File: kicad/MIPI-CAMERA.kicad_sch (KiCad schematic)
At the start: 12 parts, among them J4500 AXT530124

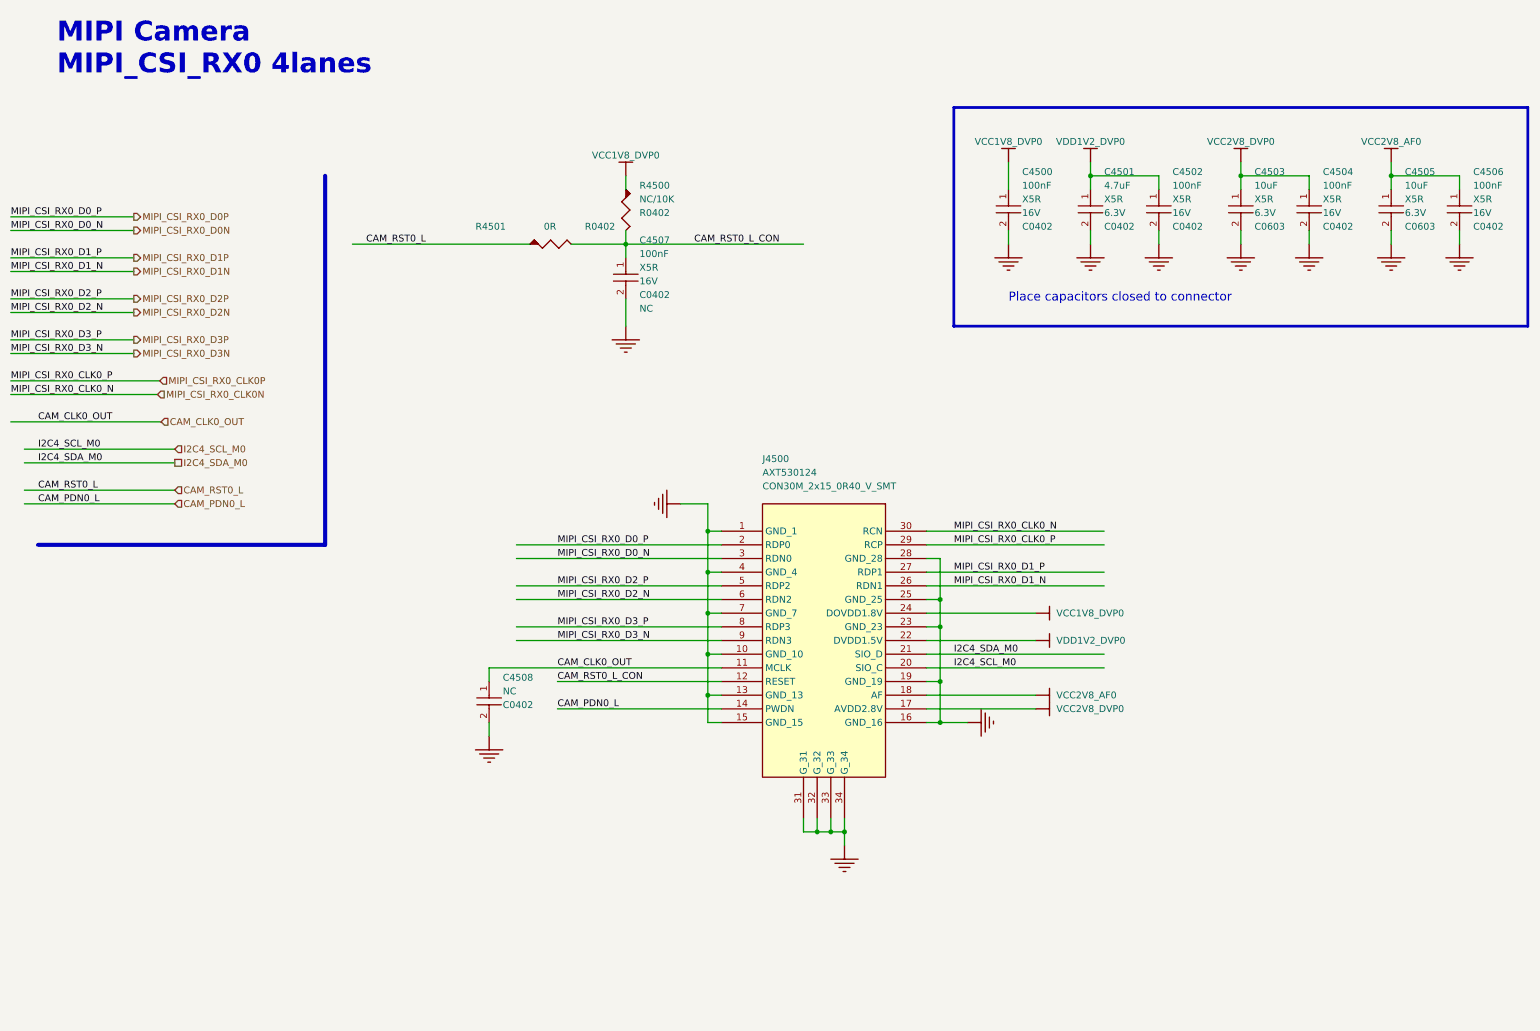
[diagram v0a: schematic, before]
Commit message: Added Pi CM4/CM5
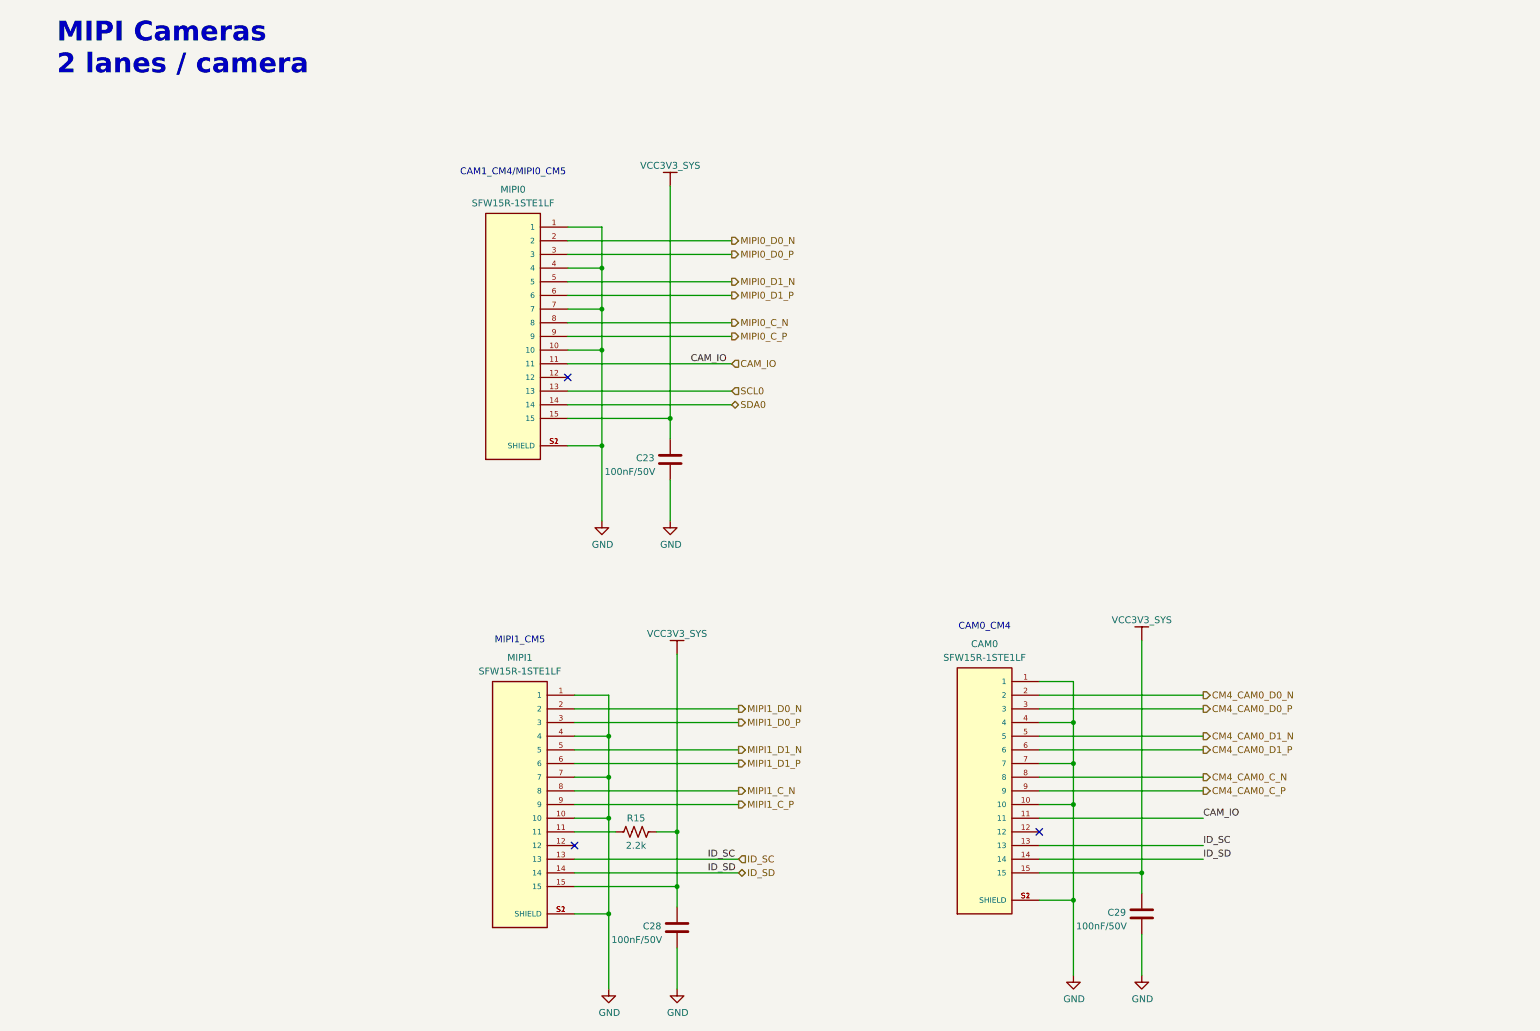
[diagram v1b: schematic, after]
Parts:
- removed C4500, C4502, C4504, C4506, C4507: 100nF, oomwoo_altium:C0402, symbol *:CAMERA_0_CAP NP_*
- removed C4501: 4.7uF, oomwoo_altium:C0402, symbol *:CAMERA_0_CAP NP_*
- removed C4503, C4505: 10uF, oomwoo_altium:C0603, symbol *:CAMERA_0_CAP NP_*
- removed C4508: NC, oomwoo_altium:C0402, symbol *:CAMERA_0_CAP NP_NC_*
- removed J4500: AXT530124, oomwoo_altium:CONN-SMD_30P-P0.40_AXT530124, symbol RK3562_REF:CAMERA_0_CMK-CB0077-FV1_2_RK3562_REF.SchLib
- removed R4500: NC/10K, Resistor_SMD:R_0402_1005Metric, symbol *:CAMERA_0_RESISTOR5_NC_*
- removed R4501: 0R, Resistor_SMD:R_0402_1005Metric, symbol *:CAMERA_1_RESISTOR5_*
- added C23, C28, C29: 100nF/50V, Capacitor_SMD:C_0603_1608Metric, symbol Device:C
- added CAM0, MIPI0, MIPI1: SFW15R-1STE1LF, SFW15R-1STE1LF:AMPHENOL_SFW15R-1STE1LF, symbol SFW15R-1STE1LF:SFW15R-1STE1LF
- added R15: 2.2k, symbol Device:R_US
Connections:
- net GND: now also C23.2, C28.2, C29.2, CAM0.1, CAM0.10, CAM0.4, CAM0.7, CAM0.S1 (SHIELD), CAM0.S2 (SHIELD), MIPI0.1, MIPI0.10, MIPI0.4, MIPI0.7, MIPI0.S1 (SHIELD), MIPI0.S2 (SHIELD), MIPI1.1, MIPI1.10, MIPI1.4, MIPI1.7, MIPI1.S1 (SHIELD), MIPI1.S2 (SHIELD)
- new net: MIPI1.11, R15.1
- new net CAM_IO: CAM0.11, MIPI0.11
- new net CM4_CAM0_C_N: CAM0.8
- new net CM4_CAM0_C_P: CAM0.9
- new net CM4_CAM0_D0_N: CAM0.2
- new net CM4_CAM0_D0_P: CAM0.3
- new net CM4_CAM0_D1_N: CAM0.5
- new net CM4_CAM0_D1_P: CAM0.6
- new net ID_SC: CAM0.13, MIPI1.13
- new net ID_SD: CAM0.14, MIPI1.14
- new net MIPI0_C_N: MIPI0.8
- new net MIPI0_C_P: MIPI0.9
- new net MIPI0_D0_N: MIPI0.2
- new net MIPI0_D0_P: MIPI0.3
- new net MIPI0_D1_N: MIPI0.5
- new net MIPI0_D1_P: MIPI0.6
- new net MIPI1_C_N: MIPI1.8
- new net MIPI1_C_P: MIPI1.9
- new net MIPI1_D0_N: MIPI1.2
- new net MIPI1_D0_P: MIPI1.3
- new net MIPI1_D1_N: MIPI1.5
- new net MIPI1_D1_P: MIPI1.6
- new net SCL0: MIPI0.13
- new net SDA0: MIPI0.14
- new net VCC3V3_SYS: C23.1, C28.1, C29.1, CAM0.15, MIPI0.15, MIPI1.15, R15.2
- no-connect marks 0 -> 3
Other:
- note added: "CAM0_CM4"
- note added: "CAM1_CM4/MIPI0_CM5"
- note added: "MIPI1_CM5"
- note removed: "Place capacitors closed to connector"

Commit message: Changed MCU to STM32G473VCT6
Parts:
- R15: footprint (none) -> Resistor_SMD:R_0603_1608Metric
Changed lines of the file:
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@@
 			)
 		)
-		(property "Footprint" ""
+		(property "Footprint" "Resistor_SMD:R_0603_1608Metric"
 			(at 263.779 268.224 90)
 			(hide yes)

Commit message: STM32G473VCT6
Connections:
- net VCC3V3_SYS renamed VCC-3V3-P
